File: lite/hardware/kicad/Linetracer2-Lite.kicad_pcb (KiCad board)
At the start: 2 copper layers, 100 x 100 mm, 30 parts, among them J1 BATTERY (AA x3, XH 2P), J2 I2C (0.96in OLED order), M1 LEFT motor FA-130RA, M2 RIGHT motor FA-130RA, Q1 2SC1815-GR, SW1 START, U1 Raspberry Pi Pico, U2 AE-TC78H653FTG

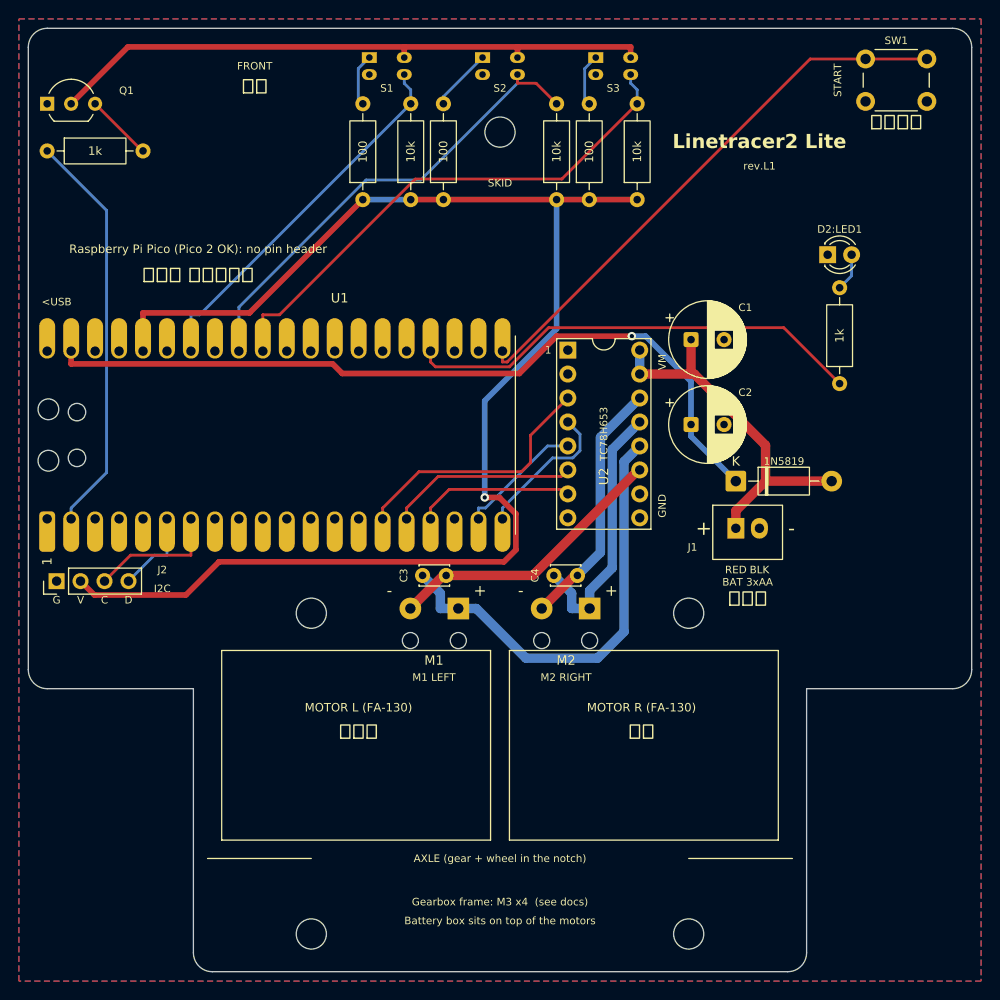
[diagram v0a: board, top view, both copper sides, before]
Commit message: Lite rev.L3: XIAO（ピンヘッダ）、ブザー、フルカラー LED 6 こ、テストパッド、手で引いた配線、車軸も印刷するギヤボックス (#4)
* Lite rev.L2: XIAO ESP32C6 と LBR-127HLD に変更、子ども向けに配置・シルクを見直し

- マイコンを Seeed Studio XIAO ESP32C6（秋月 129481）に。ピンヘッダなしで基板にじかにはんだ付け
  （自作フットプリント: 裏のテストパッドの下は銅禁止、USB の足の逃げ穴、アンテナの下は両面銅なし）
- フォトリフレクタを LBR-127HLD（秋月 104500）に。背が 5.6 mm あるのでスキッドを 7.5 mm に
  （skid_clip_h70/h75/h80.stl、ロボットは後ろに 2.9° 傾く。傾きとすき間は scad で計算）
- いらない部品: I2C の穴 J2 を削除。電池電圧の測定はなし（XIAO の ADC 3 本をセンサーで使い切る）
- ピン割り当ては ESP32-C6 の起動時の状態に合わせ、どの瞬間もモーターが回らないようにした
- 基板を 65 x 100 mm の長方形に（面積 -27%、3D プリント部品はそのまま）、抵抗を 6 mm おきに
- シルクは記号だけ（つくる順番の数字、＋、LED の絵、抵抗の 3 本目の色）。説明は手順書 lite/docs/assembly.md
- gen_3d.py の 3D モデルの位置ずれを修正（KiCad は VRML の translation に scale をかけない）
- ERC 0、DRC 0（警告 0・未接続 0）。MicroPython (ESP32_GENERIC_C6) のライブラリとサンプルを移植

Co-Authored-By: Claude Opus 5.5 <noreply@anthropic.com>

* Lite の節に、ボールキャスターは標準版用と注記

Co-Authored-By: Claude Opus 5.5 <noreply@anthropic.com>

* Lite 用ボールキャスターを追加し、3D プリント部品を子ども向けに見直した

- Lite 用ボールキャスター caster_lite_print_h70/h75/h80（玉ごと印刷、玉 φ4.0/4.5/5.0）と
  caster_lite_bead_h70/h75/h80（φ4 の玉を押し込む、先生用）。玉はスキッドの穴 (50, 11) のピンの真下。
  玉が重さで押し上げられた状態で、同じ高さのスキッドと同じ傾き・センサーと床のすき間（7.5 mm で 2.9°・2.25 mm）。
  基板設計と決めた範囲（裏 x 45〜55・y 6.5〜16、表 r 2.4）に収め、どの向きに差しても当たらない
- 干渉チェック check_caster_lite_*（sensor / bead_sensor / pcb / ball / bead_ball / floor / ballfloor / zone）と
  check_skidclip_lite_zone を追加（わざとずらした条件で検出することも確認）。-D LITE=true のときは
  check_caster_* が Lite 用キャスターを調べる。assembly は LITE_SUPPORT で skid / caster_print / caster_bead を選べる
- 子ども向け: 枠・デッキ・ツメ版デッキのツメの縦の角を丸め、車輪のふち・ハブを面取り、スキッドの角を丸めた。
  枠に L / R を刻んだ。はまる寸法は変えていない（標準版・Lite とも干渉チェックは全部「空」）
- README に Lite キャスターの節と安全の見直し表、08_knowledge に知見（玉が押し上げられる分、小さい玉ほど
  受けが床に近い、ピニオンの組み立て順の問題）を追記

Co-Authored-By: Claude Opus 5.5 <noreply@anthropic.com>

* Lite rev.L3 基板: XIAO をピンヘッダで、ブザー追加、配線を手で引き直し、シルクを改良

- XIAO ESP32C6 を 2 列 x 7 ピンのスルーホール（ピンヘッダ）に。直付け用フットプリントは削除
- 圧電スピーカー BZ1（PKM13EPYH4000-A0）＋ R9 100 Ω を赤 LED と同じ D6 に
- 自動配線をやめ、lite/scripts/layout_lite.py に配置と配線を書いた（縦・横・45°、直角は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
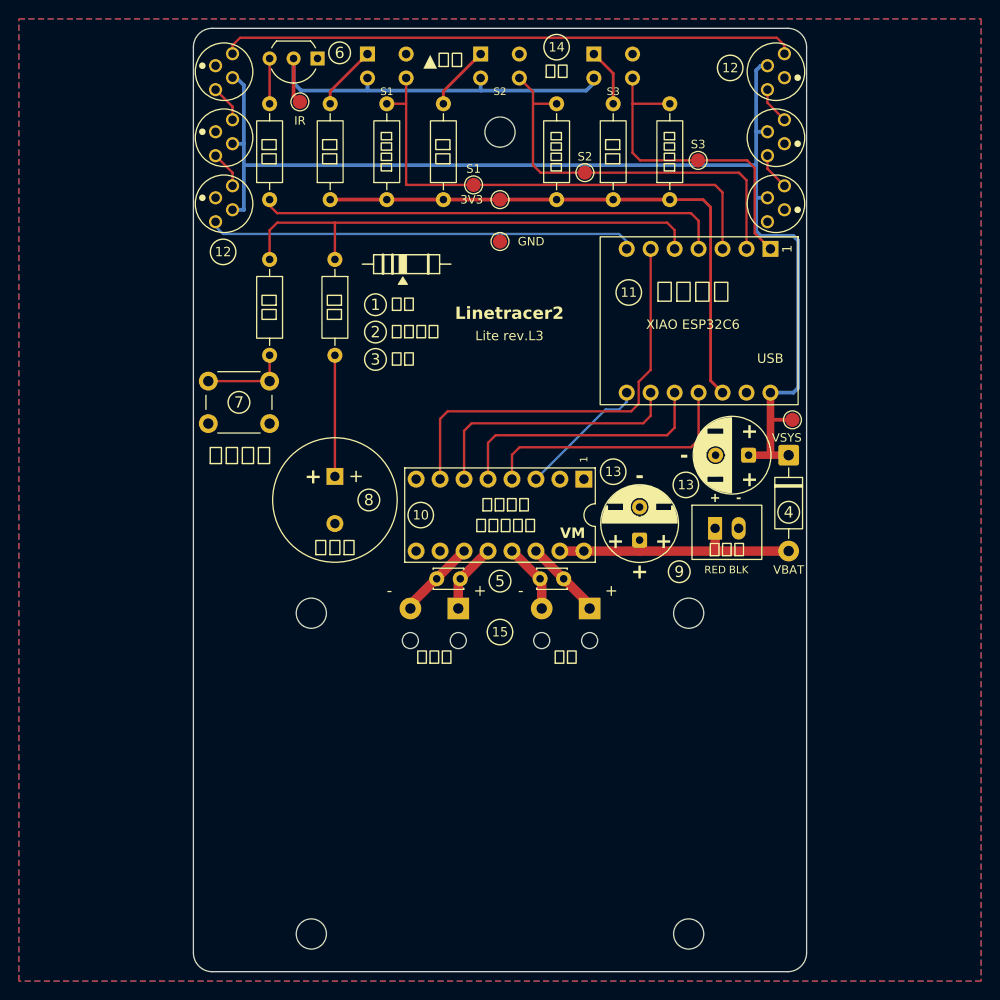
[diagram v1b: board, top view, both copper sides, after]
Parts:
- removed J2: I2C (0.96in OLED order), Connector_PinHeader_2.54mm:PinHeader_1x04_P2.54mm_Vertical
- removed R8: 1k, Resistor_THT:R_Axial_DIN0207_L6.3mm_D2.5mm_P10.16mm_Horizontal
- added BZ1: piezo 13mm, Linetracer2:Buzzer_PKM13_P5.0, F.Cu at (132.5, 97.5)
- added D3: PL9823, Linetracer2:LED_PL9823_5mm, F.Cu at (120.8, 61.6)
- added D4: PL9823, Linetracer2:LED_PL9823_5mm, F.Cu at (120.8, 54.6)
- added D5: PL9823, Linetracer2:LED_PL9823_5mm, F.Cu at (179.2, 54.6)
- added D6: PL9823, Linetracer2:LED_PL9823_5mm, F.Cu at (179.2, 61.6)
- added D7: PL9823, Linetracer2:LED_PL9823_5mm, F.Cu at (179.2, 68.6)
- added R10: 1k, Resistor_THT:R_Axial_DIN0207_L6.3mm_D2.5mm_P10.16mm_Horizontal, F.Cu at (125.6, 74.5)
- added R9: 100, Resistor_THT:R_Axial_DIN0207_L6.3mm_D2.5mm_P10.16mm_Horizontal, F.Cu at (132.5, 74.5)
- added TP1: GND, TestPoint:TestPoint_Pad_D1.5mm, F.Cu at (150.0, 72.6)
- added TP2: 3V3, TestPoint:TestPoint_Pad_D1.5mm, F.Cu at (150.0, 68.2)
- added TP3: VSYS, TestPoint:TestPoint_Pad_D1.5mm, F.Cu at (181.0, 91.5)
- added TP4: SENS1, TestPoint:TestPoint_Pad_D1.5mm, F.Cu at (147.2, 66.6)
- added TP5: SENS2, TestPoint:TestPoint_Pad_D1.5mm, F.Cu at (159.0, 65.3)
- added TP6: SENS3, TestPoint:TestPoint_Pad_D1.5mm, F.Cu at (171.0, 64.0)
- added TP7: LED_K, TestPoint:TestPoint_Pad_D1.5mm, F.Cu at (128.8, 57.8)
- D2: value LED red -> PL9823; footprint LED_THT:LED_D3.0mm -> Linetracer2:LED_PL9823_5mm
- PS1, PS2, PS3: value LBR-123F -> LBR-127HLD; footprint Linetracer2:LBR-123F -> Linetracer2:LBR-127HLD
- U1: value Raspberry Pi Pico -> XIAO ESP32C6; footprint Linetracer2:RaspberryPi_Pico_DirectSolder -> Linetracer2:XIAO_ESP32C6_Header
- moved SW1 77.6 mm to (119.1, 87.4)
- moved D2 64.2 mm to (120.8, 68.6), turned to 90 degrees
- moved U1 46.5 mm to (171.1, 81.0), turned to -90 degrees
- moved Q1 29.1 mm to (130.7, 53.2), turned to 180 degrees
- moved R7 24.1 mm to (125.6, 68.2), turned to 90 degrees
- moved C1 21.9 mm to (164.8, 104.2), turned to 90 degrees
- moved U2 14.0 mm to (150.0, 101.6), turned to -90 degrees
- moved C2 6.91 mm to (176.3, 95.2), turned to 180 degrees
- moved D1 6.24 mm to (180.6, 95.2), turned to -90 degrees
- moved C3 4.02 mm to (145.8, 108.3), turned to 180 degrees
- moved R1 3.46 mm to (132.0, 68.2)
- moved R6 3.46 mm to (168.0, 68.2)
- moved R3 2.54 mm to (162.0, 68.2)
- moved R4 2.54 mm to (138.0, 68.2)
- moved J1 2.20 mm to (172.8, 103.0)
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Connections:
- C4 pad 1: /MOT_OUT3 -> /MOT_OUT4
- C4 pad 2: /MOT_OUT4 -> /MOT_OUT3
- M2 pad 1: /MOT_OUT3 -> /MOT_OUT4
- M2 pad 2: /MOT_OUT4 -> /MOT_OUT3
- SW1 pad 1: /SW1 -> /BTN
- U1 pad 1: unconnected-(U1-GPIO0-Pad1) -> /SENS3
- U1 pad 10: unconnected-(U1-GPIO7-Pad10) -> /MOT_IN3
- U1 pad 11: unconnected-(U1-GPIO8-Pad11) -> /MOT_IN4
- U1 pad 12: unconnected-(U1-GPIO9-Pad12) -> +3V3
- U1 pad 14: unconnected-(U1-GPIO10-Pad14) -> /VSYS
- U1 pad 2: /SENS_LED_EN -> /SENS2
- U1 pad 3: GND -> /SENS1
- U1 pad 4: unconnected-(U1-GPIO2-Pad4) -> /SENS_LED_EN
- U1 pad 5: unconnected-(U1-GPIO3-Pad5) -> /SW1
- U1 pad 6: /I2C_SDA -> /MOT_IN2
- U1 pad 7: /I2C_SCL -> /RGB_DIN
- U1 pad 8: GND -> /MOT_STBY
- U1 pad 9: unconnected-(U1-GPIO6-Pad9) -> /MOT_IN1
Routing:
- net +3V3: track 152.7 -> 60.8 mm, vias 1 -> 0
- net Net-(D4-DO): track 0.00 -> 61.0 mm
- net /LED1: track 48.9 -> 0.00 mm
- net /RGB_DIN: track 0.00 -> 45.5 mm
- net /VSYS: track 83.6 -> 129.1 mm, vias 1 -> 0
- net /MOT_OUT1: track 47.5 -> 7.39 mm
- net /MOT_IN2: track 16.7 -> 45.0 mm
- net /LED_K: track 65.2 -> 43.2 mm
- net /MOT_OUT2: track 30.4 -> 8.45 mm
- net /SENS3: track 56.2 -> 34.8 mm
- net /MOT_OUT3: track 28.2 -> 7.39 mm
- net /MOT_OUT4: track 26.8 -> 8.45 mm
- net /MOT_IN3: track 13.3 -> 28.0 mm
- net /I2C_SCL: track 14.2 -> 0.00 mm
- net /SENS1: track 39.8 -> 53.2 mm
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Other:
- board size 100 x 100 mm -> 65 x 100 mm
- board text added: "+"
- board text added: "-"
- board text added: "1"
- board text added: "10"
- board text added: "11"
- board text added: "12"
- board text added: "13"
- board text added: "14"
- board text added: "15"
- board text added: "2"
- board text added: "3"
- board text added: "3V3"
- board text added: "4"
- board text added: "5"
- board text added: "6"
- board text added: "7"
- board text added: "8"
- board text added: "9"
- board text added: "GND"
- board text added: "IR"
- board text added: "Linetracer2"
- board text added: "Lite rev.L3"
- board text added: "USB"
- board text added: "VBAT"
- board text added: "VM"
- board text added: "VSYS"
- board text added: "XIAO ESP32C6"
- board text added: "XIAO ESP32C6 + TC78H653FTG + FA-130 x2"
- board text added: "rev.L3 2026-10 EDTC"
- board text added: "▲まえ"
- board text added: "あか"
- board text added: "うら"
- board text added: "こどもむけ ライントレーサー"
- board text added: "だいだい"
- board text added: "ちゃ"
- board text added: "キャスター"
- board text added: "センサー"
- board text added: "ドライバー"
- board text added: "ブザー"
- board text added: "マイコン"
- board text added: "モーター"
- board text removed: "<USB"
- board text removed: "AXLE (gear + wheel in the notch)"
- board text removed: "BAT 3xAA"
- board text removed: "Battery box sits on top of the motors"
- board text removed: "C"
- board text removed: "D"
- board text removed: "D2:LED1"
- board text removed: "FRONT"
- board text removed: "G"
- board text removed: "Gearbox frame: M3 x4 (see docs)"
- board text removed: "I2C"
- board text removed: "M1 LEFT"
- board text removed: "M2 RIGHT"
- board text removed: "MOTOR L (FA-130)"
- board text removed: "MOTOR R (FA-130)"
- board text removed: "Raspberry Pi Pico (Pico 2 OK): no pin header"
- board text removed: "Raspberry Pi Pico + TC78H653FTG + FA-130 x2"
- board text removed: "SENSOR SIDE: LBR-123F x3 (lens to the floor)"
- board text removed: "SKID"
- board text removed: "START"
- board text removed: "V"
- board text removed: "rev.L1"
- board text removed: "rev.L1 2026-10 EDTC"
- board text removed: "じかに はんだづけ"
- board text removed: "まえ"
- board text removed: "センサーはこちらの面に付ける"
- board text removed: "子ども向けライントレーサー教材"
